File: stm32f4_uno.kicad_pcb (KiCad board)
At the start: 2 copper layers, 68.6 x 53.3 mm, 58 parts, among them J101 Digital/PWM, J102 Power, J103 Analog, J104 Digital/PWM, J105 Conn_ST_STDC14, J401 TYPE-C-31-M-12, U101 STM32F407VGTx, U201 AMS1117-5.0, U301 XC6206P332MR, U501 W25Q128JVSIQ, Y101 25MHz, Y102 32.768kHz

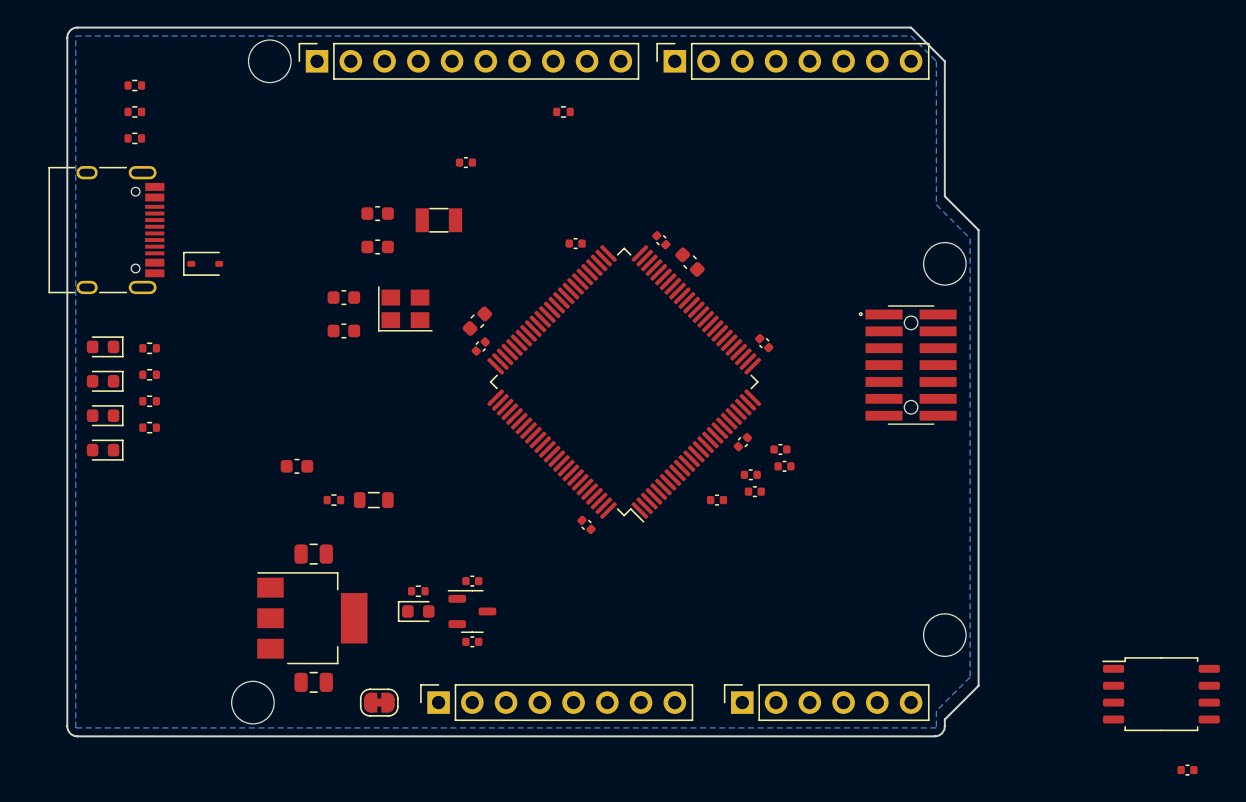
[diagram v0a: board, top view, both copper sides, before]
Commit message: Finish schematic with all pins
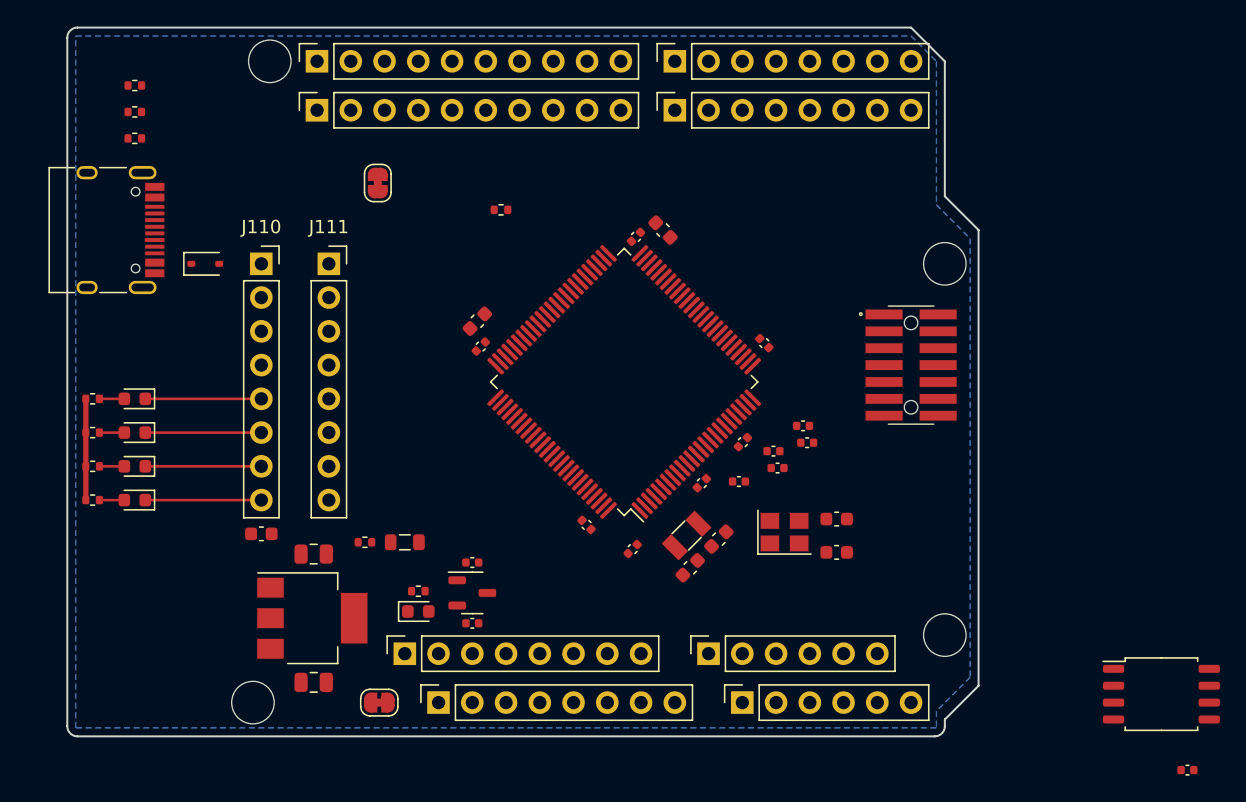
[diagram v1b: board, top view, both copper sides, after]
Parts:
- added J106: Ethernet, Connector_PinSocket_2.54mm:PinSocket_1x10_P2.54mm_Vertical, F.Cu at (118.8, 52.9)
- added J107: Digital/PWM, Connector_PinSocket_2.54mm:PinSocket_1x08_P2.54mm_Vertical, F.Cu at (145.7, 52.9)
- added J108: Analog, Connector_PinSocket_2.54mm:PinSocket_1x06_P2.54mm_Vertical, F.Cu at (148.3, 93.8)
- added J109: Power, Connector_PinSocket_2.54mm:PinSocket_1x08_P2.54mm_Vertical, F.Cu at (125.4, 93.8)
- added J110: Digital/PWM, Connector_PinSocket_2.54mm:PinSocket_1x08_P2.54mm_Vertical, F.Cu at (114.6, 64.4)
- added J111: Digital/PWM, Connector_PinSocket_2.54mm:PinSocket_1x08_P2.54mm_Vertical, F.Cu at (119.7, 64.4)
- added JP102: Jumper_2_Bridged, Jumper:SolderJumper-2_P1.3mm_Bridged_RoundedPad1.0x1.5mm, F.Cu at (123.4, 58.4)
- moved C102 40.7 mm to (157.9, 83.6)
- moved C103 40.7 mm to (157.9, 86.2)
- moved C104 35.5 mm to (146.9, 87.3), turned to -135 degrees
- moved C105 33.8 mm to (149.0, 85.2), turned to 45 degrees
- moved Y101 33.1 mm to (154.0, 84.6)
- moved C115 31.7 mm to (142.5, 85.9), turned to -135 degrees
- moved Y102 30.2 mm to (146.6, 84.9), turned to 45 degrees
- moved C111 20.4 mm to (147.8, 81.0), turned to -135 degrees
- moved R101 8.74 mm to (132.6, 60.4)
- moved R102 6.93 mm to (101.9, 82.2)
- moved R103 6.51 mm to (101.9, 79.7)
- moved R104 6.11 mm to (101.9, 77.1)
- moved C112 5.74 mm to (114.6, 84.8)
- moved R105 5.73 mm to (101.9, 74.6)
- moved D104 4.58 mm to (105.1, 74.6)
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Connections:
- net /USB/VBUS renamed /VBUS
- net /VCAP_1 renamed /CAP_1
- net /VCAP_2 renamed /CAP_2
- net Net-(J401-CC1) renamed /USB/CC1
- net Net-(J401-CC2) renamed /USB/CC2
- C116 pad 1: /VDDA -> /VREF+
- C117 pad 1: /VDDA -> /VREF+
- D101 pad 1: /LED1_GRN -> /PD3/LED1_GRN
- D102 pad 1: /LED2_ORG -> /PD1/LED2_ORG
- D103 pad 1: /LED3_RED -> /PC12/LED3_RED
- D104 pad 1: /LED4_BLU -> /PC10/LED4_BLU
- J101 pad 1: /SCL/A5 -> /PB6
- J101 pad 10: /8 -> /PD8
- J101 pad 2: /SDA/A4 -> /PB9
- J101 pad 3: /AREF -> /VREF+
- J101 pad 5: /13 -> /PD11
- J101 pad 6: /12 -> /PD10
- J101 pad 7: /*11 -> /PD13
- J101 pad 8: /*10 -> /PD12
- J101 pad 9: /*9 -> /PB15
- J102 pad 2: /IOREF -> +3V3
- J103 pad 1: /A0 -> /PE2
- J103 pad 2: /A1 -> /PE4
- J103 pad 3: /A2 -> /PE6
- J103 pad 4: /A3 -> /PC0
- J103 pad 5: /SDA/A4 -> /PB9
- J103 pad 6: /SCL/A5 -> /PB6
- J104 pad 1: /7 -> /PE15
- J104 pad 2: /*6 -> /PE13
- J104 pad 3: /*5 -> /PE11
- J104 pad 4: /4 -> /PE8
- J104 pad 5: /*3 -> /PE9
- J104 pad 6: /2 -> /PB1
- J104 pad 7: /TX/1 -> /PB10
- J104 pad 8: /RX/0 -> /PD9
- U101 pad 1: unconnected-(U101-PE2-Pad1) -> /PE2
- U101 pad 15: /ETH_MDC -> /PC0
- U101 pad 16: unconnected-(U101-PC1-Pad16) -> /ETH_MDC
- U101 pad 17: unconnected-(U101-PC2-Pad17) -> /PC2
- U101 pad 18: unconnected-(U101-PC3-Pad18) -> /PC3
- U101 pad 2: unconnected-(U101-PE3-Pad2) -> /PE3
- U101 pad 21: /VDDA -> /VREF+
- U101 pad 23: unconnected-(U101-PA0-Pad23) -> /PA0
- U101 pad 26: unconnected-(U101-PA3-Pad26) -> /PA3
- U101 pad 3: unconnected-(U101-PE4-Pad3) -> /PE4
- U101 pad 35: unconnected-(U101-PB0-Pad35) -> /PB0
- U101 pad 36: unconnected-(U101-PB1-Pad36) -> /PB1
- U101 pad 37: unconnected-(U101-PB2-Pad37) -> /PB2
- U101 pad 38: unconnected-(U101-PE7-Pad38) -> /PE7
- U101 pad 39: unconnected-(U101-PE8-Pad39) -> /PE8
- U101 pad 4: unconnected-(U101-PE5-Pad4) -> /PE5
- U101 pad 40: unconnected-(U101-PE9-Pad40) -> /PE9
- U101 pad 41: unconnected-(U101-PE10-Pad41) -> /PE10
- U101 pad 42: unconnected-(U101-PE11-Pad42) -> /PE11
- U101 pad 43: unconnected-(U101-PE12-Pad43) -> /PE12
- U101 pad 44: unconnected-(U101-PE13-Pad44) -> /PE13
- U101 pad 45: unconnected-(U101-PE14-Pad45) -> /PE14
- U101 pad 46: unconnected-(U101-PE15-Pad46) -> /PE15
- U101 pad 47: unconnected-(U101-PB10-Pad47) -> /PB10
- U101 pad 5: unconnected-(U101-PE6-Pad5) -> /PE6
- U101 pad 53: unconnected-(U101-PB14-Pad53) -> /PB14
- U101 pad 54: unconnected-(U101-PB15-Pad54) -> /PB15
- U101 pad 55: unconnected-(U101-PD8-Pad55) -> /PD8
- U101 pad 56: unconnected-(U101-PD9-Pad56) -> /PD9
- U101 pad 57: unconnected-(U101-PD10-Pad57) -> /PD10
- U101 pad 58: unconnected-(U101-PD11-Pad58) -> /PD11
- U101 pad 59: unconnected-(U101-PD12-Pad59) -> /PD12
- U101 pad 60: unconnected-(U101-PD13-Pad60) -> /PD13
- U101 pad 61: unconnected-(U101-PD14-Pad61) -> /PD14
- U101 pad 62: unconnected-(U101-PD15-Pad62) -> /PD15
- U101 pad 63: unconnected-(U101-PC6-Pad63) -> /PC6
- U101 pad 64: unconnected-(U101-PC7-Pad64) -> /PC7
- U101 pad 65: unconnected-(U101-PC8-Pad65) -> /PC8
- U101 pad 66: unconnected-(U101-PC9-Pad66) -> /PC9
- U101 pad 67: unconnected-(U101-PA8-Pad67) -> /PA8
- U101 pad 7: unconnected-(U101-PC13-Pad7) -> /PC13
- U101 pad 77: unconnected-(U101-PA15-Pad77) -> /PA15
- U101 pad 78: unconnected-(U101-PC10-Pad78) -> /PC10/LED4_BLU
- U101 pad 79: unconnected-(U101-PC11-Pad79) -> /PC11
- U101 pad 80: unconnected-(U101-PC12-Pad80) -> /PC12/LED3_RED
- U101 pad 81: unconnected-(U101-PD0-Pad81) -> /PD0
- U101 pad 82: unconnected-(U101-PD1-Pad82) -> /PD1/LED2_ORG
- U101 pad 83: unconnected-(U101-PD2-Pad83) -> /PD2
- U101 pad 84: unconnected-(U101-PD3-Pad84) -> /PD3/LED1_GRN
- U101 pad 85: unconnected-(U101-PD4-Pad85) -> /PD4
- U101 pad 86: unconnected-(U101-PD5-Pad86) -> /PD5
- U101 pad 87: unconnected-(U101-PD6-Pad87) -> /PD6
- U101 pad 88: unconnected-(U101-PD7-Pad88) -> /PD7
- U101 pad 90: unconnected-(U101-PB4-Pad90) -> /PB4
- U101 pad 92: unconnected-(U101-PB6-Pad92) -> /PB6
- U101 pad 95: unconnected-(U101-PB8-Pad95) -> /PB8
- U101 pad 96: unconnected-(U101-PB9-Pad96) -> /PB9
- U101 pad 97: unconnected-(U101-PE0-Pad97) -> /PE0
- U101 pad 98: unconnected-(U101-PE1-Pad98) -> /PE1
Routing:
- net /PD3/LED1_GRN: track 0.00 -> 8.74 mm
- net /PD1/LED2_ORG: track 0.00 -> 8.74 mm
- net /PC12/LED3_RED: track 0.00 -> 8.74 mm
- net /PC10/LED4_BLU: track 0.00 -> 8.74 mm
- net +3V3: track 0.00 -> 7.62 mm
- net Net-(D104-A): track 0.00 -> 1.88 mm
- net Net-(D103-A): track 0.00 -> 1.88 mm
- net Net-(D102-A): track 0.00 -> 1.88 mm
- net Net-(D101-A): track 0.00 -> 1.88 mm

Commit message: WIP
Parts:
- removed J401: TYPE-C-31-M-12, Connector_USB:USB_C_Receptacle_HRO_TYPE-C-31-M-12
- added J1: Barrel_Jack, Connector_BarrelJack:BarrelJack_CUI_PJ-102AH_Horizontal, F.Cu at (110.8, 92.4)
- added J2: SHOU HAN TYPE-C 16PIN 2MD(073) (C2765186), Project_Library:SHOU HAN TYPE-C 16PIN 2MD(073) (C2765186), F.Cu at (103.7, 61.9)
- J105: footprint Connector_Samtec:Samtec_FTSH-107-XX-YYY-DV-K-A -> Project_Library:Samtec_FTSH-107-XX-YYY-DV-K
- U301: footprint Package_TO_SOT_SMD:SOT-23-3 -> Package_TO_SOT_SMD:SOT-23
- U501: value W25Q128JVSIQ -> SST26VF016BEUI-104I/SN; footprint Package_SO:SOIC-8_5.23x5.23mm_P1.27mm -> Package_SO:SOIC-8_3.9x4.9mm_P1.27mm
- moved C501 52.3 mm to (167.6, 53.0), turned to -135 degrees
- moved JP102 47.4 mm to (165.5, 79.9)
- moved U501 42.2 mm to (173.0, 55.7), turned to -135 degrees
- moved R106 37.0 mm to (157.8, 74.6), turned to -90 degrees
- moved L101 35.2 mm to (157.8, 71.6), turned to 90 degrees
- moved R301 24.3 mm to (102.5, 84.8), turned to 0 degrees
- moved R101 22.5 mm to (137.1, 82.5), turned to -135 degrees
- moved D301 22.1 mm to (105.1, 84.8)
- moved C112 13.4 mm to (127.9, 83.4), turned to 180 degrees
- moved C201 9.37 mm to (123.2, 87.8), turned to 90 degrees
- moved C104 8.39 mm to (155.3, 87.6)
- moved C105 8.39 mm to (157.4, 85.4)
- moved Y102 8.39 mm to (155.0, 85.1)
- moved C202 5.19 mm to (113.6, 87.8), turned to -90 degrees
- moved C115 4.96 mm to (146.4, 82.7), turned to -45 degrees
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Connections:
- J103 pad 1: /PE2 -> /PE3
- J103 pad 2: /PE4 -> /PE5
- J103 pad 3: /PE6 -> /PC13
- J103 pad 4: /PC0 -> /PC2
- J106 pad 10: /ETH_RXD1 -> /ETH_MDC
- J106 pad 2: /ETH_REF_CLK -> /ETH_TXD1
- J106 pad 3: /ETH_MDIO -> /ETH_TXD0
- J106 pad 4: /ETH_CRS_DV -> /ETH_TX_EN
- J106 pad 5: /ETH_TX_EN -> /ETH_RXD1
- J106 pad 6: /ETH_TXD0 -> /ETH_RXD0
- J106 pad 7: /ETH_TXD1 -> /ETH_CRS_DV
- J106 pad 8: /ETH_MDC -> /ETH_MDIO
- J106 pad 9: /ETH_RXD0 -> /ETH_REF_CLK
- J108 pad 1: /PE3 -> /PE2
- J108 pad 2: /PE5 -> /PE4
- J108 pad 3: /PC13 -> /PE6
- J108 pad 4: /PC2 -> /PC0
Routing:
- net /PB6: track 0.00 -> 106.3 mm, vias 0 -> 1
- net /PB9: track 0.00 -> 99.3 mm, vias 0 -> 1
- net /~{RESET}: track 0.00 -> 82.2 mm
- net +5V: track 0.00 -> 58.4 mm, vias 0 -> 1
- net /VBAT: track 0.00 -> 58.3 mm, vias 0 -> 1
- net /V_{IN}: track 0.00 -> 55.5 mm
- net +3V3: track 7.62 -> 62.0 mm
- net GND: track 0.00 -> 50.0 mm, vias 0 -> 14
- net /ETH_MDC: track 0.00 -> 39.6 mm
- net /ETH_MDIO: track 0.00 -> 32.4 mm
- net /ETH_REF_CLK: track 0.00 -> 32.2 mm
- net /ETH_RXD1: track 0.00 -> 31.4 mm
- net /ETH_RXD0: track 0.00 -> 29.6 mm
- net /ETH_TX_EN: track 0.00 -> 28.2 mm
- net /PD11: track 0.00 -> 27.9 mm, vias 0 -> 1
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
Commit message: WIP
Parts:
- D301: value LED green (PWR) -> PWR
- JP102: moved to B.Cu
- moved J107 26.9 mm to (118.8, 54.3)
- moved J106 21.8 mm to (140.6, 54.3)
- moved U501 18.6 mm to (156.5, 64.1), turned to 180 degrees
- moved C501 11.7 mm to (161.3, 62.9), turned to -90 degrees
- moved R402 11.4 mm to (110.4, 63.1), turned to 90 degrees
- moved R403 10.4 mm to (111.5, 63.1), turned to 90 degrees
- moved R401 10.2 mm to (110.4, 59.7), turned to -90 degrees
- moved JP102 9.96 mm to (156.0, 77.0), turned to 180 degrees
- moved D105 6.18 mm to (105.8, 69.0), turned to 180 degrees
- moved R106 2.39 mm to (155.5, 75.2)
- moved L101 2.11 mm to (156.6, 73.3), turned to 0 degrees
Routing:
- net +3V3: track 62.0 -> 211.4 mm, vias 0 -> 4
- net /~{RESET}: track 82.2 -> 1.69 mm
- net /VREF+: track 3.53 -> 76.2 mm, vias 0 -> 1
- net /PD9: track 0.00 -> 42.3 mm, vias 0 -> 1
- net /PB10: track 0.00 -> 38.4 mm, vias 0 -> 1
- net /PB9: track 99.3 -> 137.5 mm, vias 1 -> 0
- net /PB6: track 106.3 -> 144.4 mm, vias 1 -> 0
- net /PB14: track 0.00 -> 37.5 mm, vias 0 -> 1
- net /USB_OTG_FS_D+: track 0.00 -> 37.2 mm, vias 0 -> 2
- net /USB_OTG_FS_D-: track 0.00 -> 36.3 mm, vias 0 -> 2
- net /USART1_RX: track 0.00 -> 34.9 mm, vias 0 -> 2
- net /PE14: track 0.00 -> 34.0 mm, vias 0 -> 1
- net /SPI1_MOSI: track 0.00 -> 33.8 mm
- net /SYS_SWCLK: track 0.00 -> 30.2 mm, vias 0 -> 2
- net /SYS_SWDIO: track 0.00 -> 29.7 mm, vias 0 -> 2
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
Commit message: First version done
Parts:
- D301: value PWR -> LED green (PWR)
- J107, J110, J111: value Digital/PWM -> STM32 GPIO
- J108: value Analog -> STM32 GPIO
- J109: value Power -> STM32 GPIO
- moved C501 1.48 mm to (161.2, 61.4)
- moved U501 1.35 mm to (156.5, 62.8)
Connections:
- J1 pad 3: (no net) -> unconnected-(J1-Pad3)
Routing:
- net /~{RESET}: track 1.69 -> 65.6 mm, vias 0 -> 4
- net /USART1_TX: track 0.00 -> 43.0 mm, vias 0 -> 2
- net +3V3: track 211.4 -> 239.1 mm, vias 4 -> 12
- net /PA3: track 28.9 -> 40.2 mm, vias 1 -> 3
- net /PC3: track 25.6 -> 31.6 mm, vias 1 -> 2
- net /PC2: track 24.7 -> 30.0 mm, vias 1 -> 2
- net /PA0: track 32.5 -> 27.4 mm, vias 1 -> 2
- net /PC0: track 17.8 -> 21.7 mm, vias 1 -> 2
- net /PE1: track 12.9 -> 15.7 mm
- net /USART1_RX: track 34.9 -> 37.6 mm
- net /SPI1_NSS: track 13.9 -> 11.5 mm
- net /VBAT: track 58.3 -> 56.0 mm
- net /V_{IN}: track 55.5 -> 53.3 mm
- net /PD9: track 42.3 -> 44.4 mm
- net /PE0: track 12.2 -> 13.8 mm
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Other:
- board text added: "LED1"
- board text added: "LED2"
- board text added: "LED3"
- board text added: "LED4"
- board text added: "V_{IN} 6V..15V"

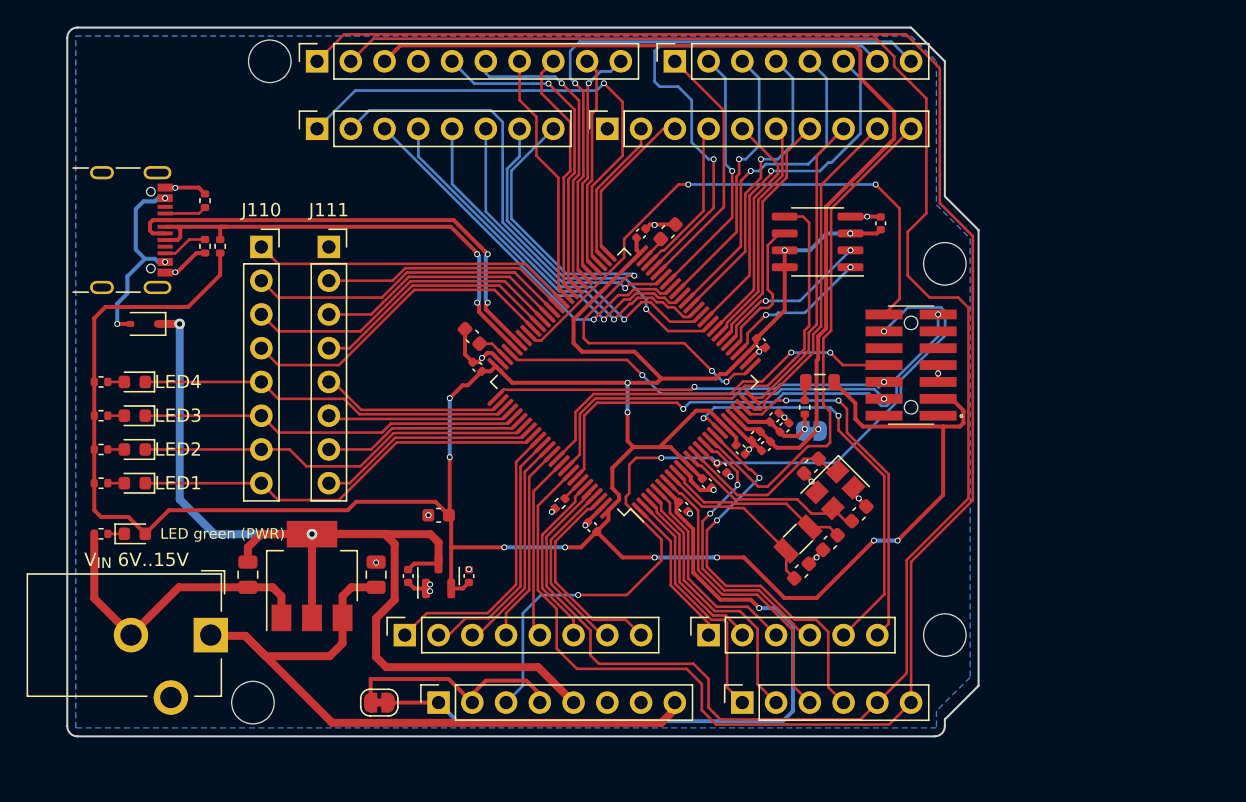
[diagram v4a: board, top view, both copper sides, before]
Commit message: Add ETH_RXER
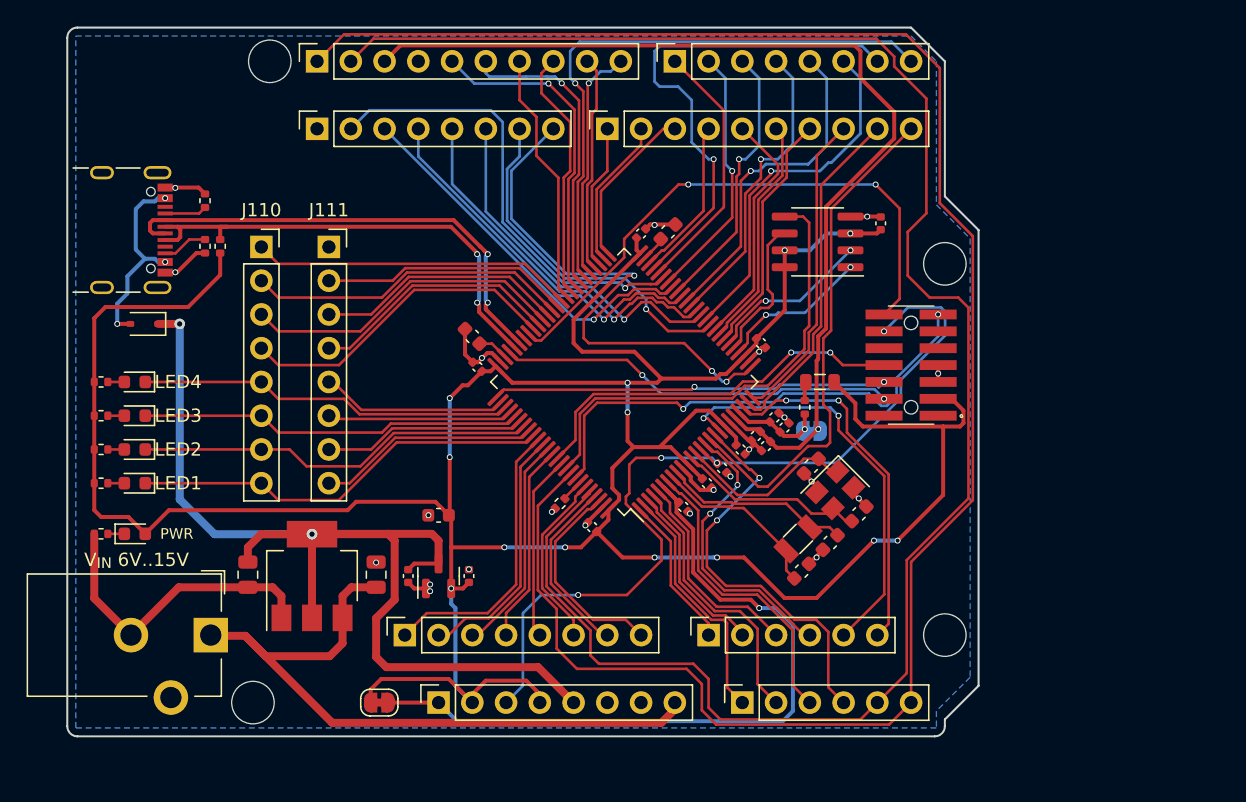
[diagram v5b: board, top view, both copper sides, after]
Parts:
- D301: value LED green (PWR) -> PWR
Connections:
- J106 pad 1: GND -> /ETH_RXER
- J107 pad 1: /PB14 -> GND
- U101 pad 53: /PB14 -> /ETH_RXER
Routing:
- net /PB14: track 38.3 -> 0.00 mm, vias 1 -> 0
- net /ETH_RXER: track 0.00 -> 10.8 mm
- net +3V3: track 239.1 -> 247.9 mm, vias 12 -> 13

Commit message: Replace 3V3 LDO for a 1A model
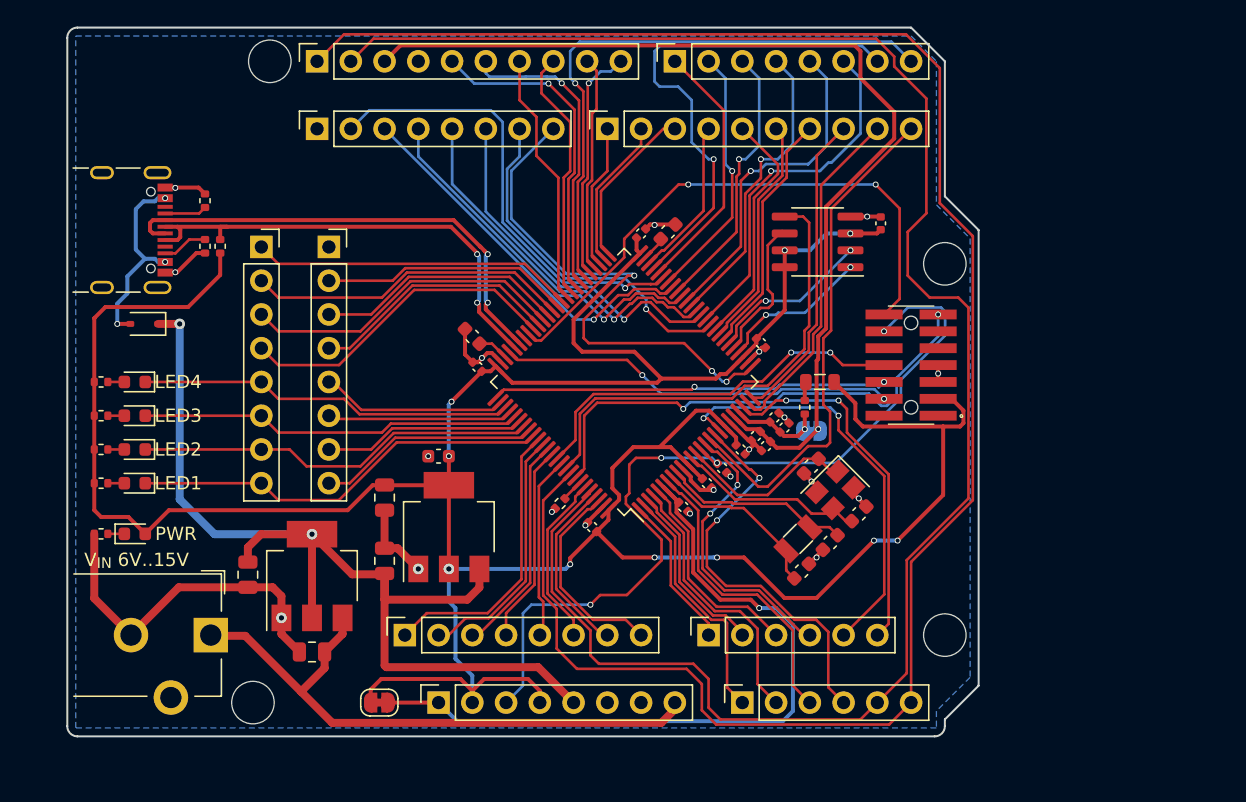
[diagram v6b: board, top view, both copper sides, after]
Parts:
- C301, C302: value 1u 25V -> 22u 25V; footprint Capacitor_SMD:C_0402_1005Metric -> Capacitor_SMD:C_0805_2012Metric
- D301: value PWR -> LED green (PWR)
- U301: value XC6206P332MR -> AMS1117-3.3; footprint Package_TO_SOT_SMD:SOT-23 -> Package_TO_SOT_SMD:SOT-223-3_TabPin2
- moved C302 8.67 mm to (123.9, 82.0), turned to -90 degrees
- moved C201 7.56 mm to (118.4, 93.6), turned to 180 degrees
- moved C112 4.45 mm to (127.9, 78.9)
- moved U301 3.76 mm to (128.7, 84.3)
- moved C301 2.11 mm to (123.9, 86.8), turned to 90 degrees
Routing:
- net /V_{IN}: track 53.3 -> 45.4 mm
- net GND: track 60.3 -> 68.0 mm, vias 22 -> 20
- net +5V: track 84.5 -> 78.4 mm
- net +3V3: track 247.9 -> 243.2 mm, vias 13 -> 10
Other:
- board text added: "PWR"
